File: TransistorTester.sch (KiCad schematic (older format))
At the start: 31 parts, among them IC1 ATMEGA8-P, IC2 78L05, J1 3-pin Header, T1 BC547, T2 BC547, T3 BC557

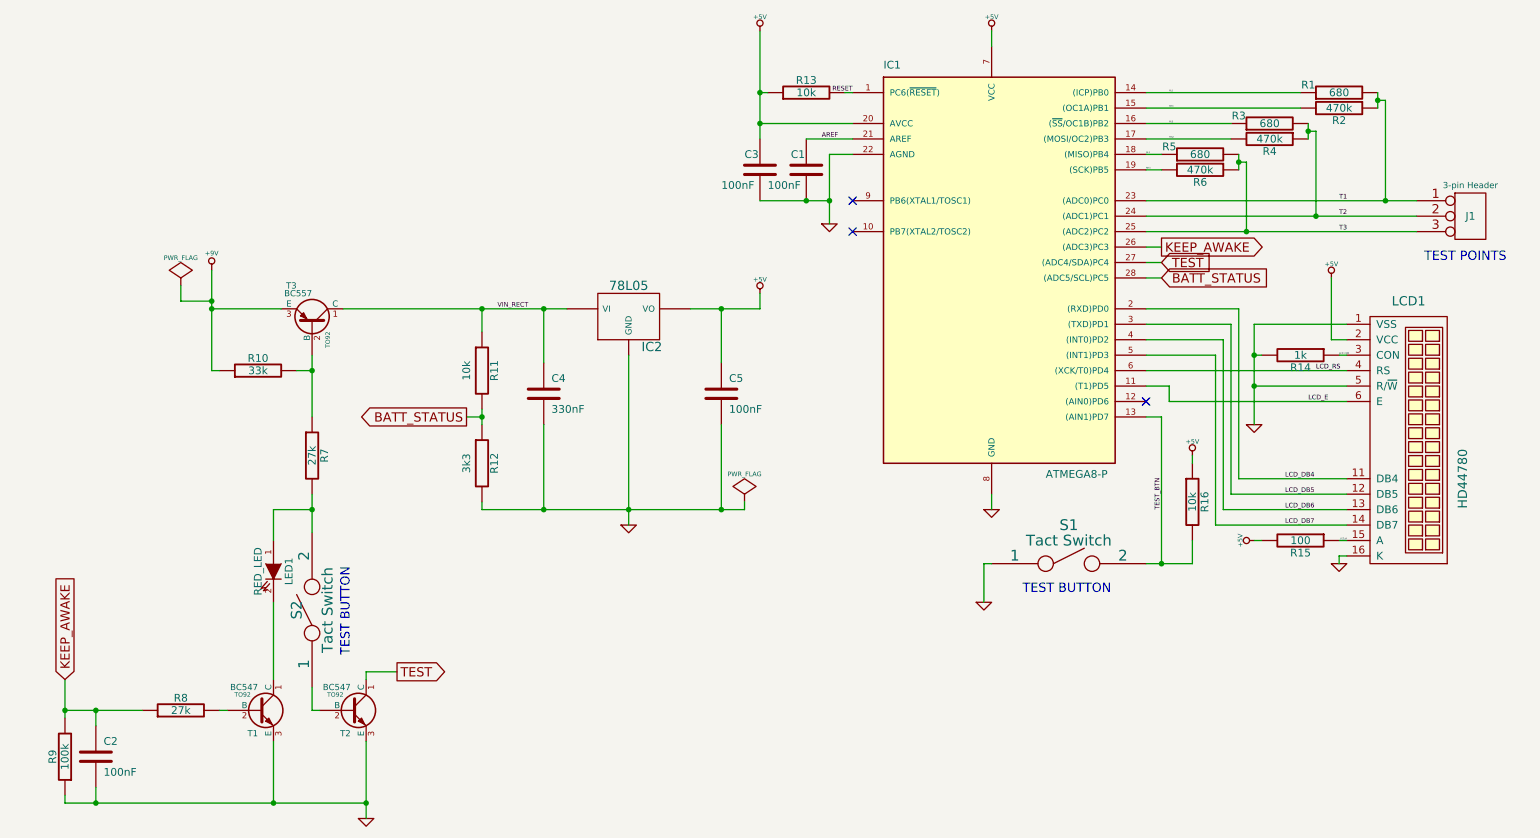
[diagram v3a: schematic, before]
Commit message: v.B.0.2: No jumper, fat tracks, horizontal Rs
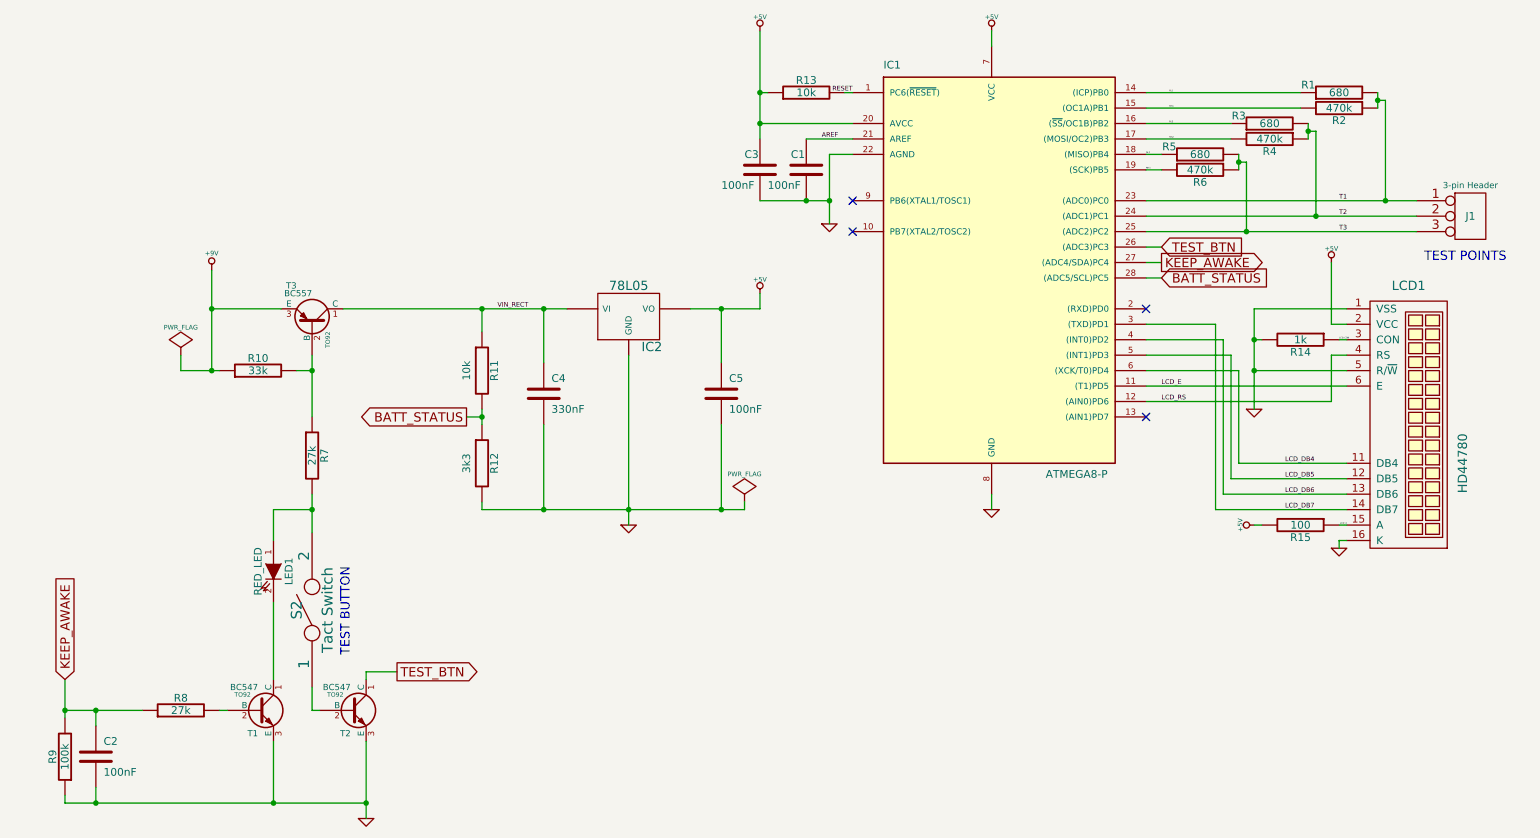
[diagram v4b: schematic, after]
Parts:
- removed R16: 10k, symbol R
- removed S1: Tact Switch, symbol SPST
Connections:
- net KEEP_AWAKE: now also IC1.27 ((ADC4/SDA)PC4); no longer IC1.26 ((ADC3)PC3)
- net LCD_DB4: now also IC1.6 ((XCK/T0)PD4); no longer IC1.2 ((RXD)PD0)
- net LCD_DB5: now also IC1.5 ((INT1)PD3); no longer IC1.3 ((TXD)PD1)
- net LCD_DB7: now also IC1.3 ((TXD)PD1); no longer IC1.5 ((INT1)PD3)
- net LCD_RS: now also IC1.12 ((AIN0)PD6); no longer IC1.6 ((XCK/T0)PD4)
- net TEST_BTN: now also IC1.26 ((ADC3)PC3), T2.1 (C); no longer IC1.13 ((AIN1)PD7)
- removed net TEST: IC1.27 ((ADC4/SDA)PC4), T2.1 (C)
- no-connect marks 3 -> 4
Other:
- moved on the sheet: LCD1, R14, R15
